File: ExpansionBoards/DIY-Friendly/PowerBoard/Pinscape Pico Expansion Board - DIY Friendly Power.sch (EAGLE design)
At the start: 75 parts, among them IC1 UCC27524P, IC10 ULN2803A, IC11 ULN2803A, IC12 ULN2803A, IC13 DS1307+, IC2 UCC27524P, IC3 UCC27524P, IC4 UCC27524P, IC5 UCC27524P, IC6 UCC27524P, IC7 UCC27524P, IC8 UCC27524P, IC9 ULN2803A, J1 640445-4, J15 SSQ-108-02-T-S-RA, J2 640445-9, J3 640445-9, J4 1-640456-0, J5 1-640456-0, J6 1-640456-0, J7 1-640456-0, Q1 FDPF085N10A, Q10 FDPF085N10A, Q11 FDPF085N10A, Q12 FDPF085N10A, Q13 FDPF085N10A, Q14 FDPF085N10A, Q15 FDPF085N10A, Q16 FDPF085N10A, Q2 FDPF085N10A, Q3 FDPF085N10A, Q4 FDPF085N10A, Q5 FDPF085N10A, Q6 FDPF085N10A, Q7 FDPF085N10A, Q8 FDPF085N10A, Q9 FDPF085N10A, Y1 ECS-.327-12.5-13X-C

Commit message: expansion board improvements
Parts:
- J1: value 640445-4 -> 640445-6; device SamacSys_Parts:640445-4 -> SamacSys_Parts:640445-6
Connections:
- net 12V: now also J1.5; no longer J1.3
- net 5V: now also J1.6; no longer J1.4
- net GND: now also J1.3, J1.4
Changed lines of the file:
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@@
 <attribute name="PARTNO" value="810-FG14X5R1H475KRT0"/>
 </part>
-<part name="J1" library="SamacSys_Parts" deviceset="640445-4" device=""/>
+<part name="J1" library="SamacSys_Parts" deviceset="640445-6" device=""/>
 <part name="J15" library="SamacSys_Parts" deviceset="SSQ-108-02-T-S-RA" device=""/>
 <part name="D2" library="SamacSys_Parts" deviceset="SB140-T" device=""/>
@@
 <text x="96.52" y="168.148" size="2.54" layer="91" align="center">Worker Pico 1</text>
 <text x="96.52" y="81.788" size="2.54" layer="91" align="center">Worker Pico 2</text>
-<text x="193.04" y="167.64" size="2.54" layer="91" align="center">Secondary PSU Power Input</text>
+<text x="193.04" y="172.72" size="2.54" layer="91" align="center">Secondary PSU Power Input</text>
 <text x="193.04" y="147.32" size="2.54" layer="91" align="center">Cross-Board Signals</text>
 </plain>
@@
 <instance part="PICO2" gate="G$1" x="96.52" y="45.72"/>
 <instance part="D1" gate="G$1" x="119.38" y="68.58"/>
-<instance part="J1" gate="G$1" x="182.88" y="162.56" smashed="yes">
-<attribute name="NAME" x="199.39" y="165.1" size="1.778" layer="95" align="center-left"/>
-<attribute name="VALUE" x="199.39" y="162.56" size="1.778" layer="96" align="center-left"/>
+<instance part="J1" gate="G$1" x="182.88" y="167.64" smashed="yes">
+<attribute name="NAME" x="199.39" y="170.18" size="1.778" layer="95" align="center-left"/>
+<attribute name="VALUE" x="199.39" y="167.64" size="1.778" layer="96" align="center-left"/>
 </instance>
 <instance part="J15" gate="G$1" x="182.88" y="139.7" smashed="yes">
@@
 <segment>
 <pinref part="J1" gate="G$1" pin="2"/>
-<wire x1="180.34" y1="160.02" x2="182.88" y2="160.02" width="0.1524" layer="91"/>
-<label x="177.8" y="162.56" size="1.27" layer="95" rot="R180" xref="yes"/>
+<wire x1="180.34" y1="165.1" x2="182.88" y2="165.1" width="0.1524" layer="91"/>
+<label x="177.8" y="167.64" size="1.27" layer="95" rot="R180" xref="yes"/>
 <pinref part="J1" gate="G$1" pin="1"/>
-<wire x1="177.8" y1="162.56" x2="180.34" y2="162.56" width="0.1524" layer="91"/>
+<wire x1="177.8" y1="167.64" x2="180.34" y2="167.64" width="0.1524" layer="91"/>
+<wire x1="180.34" y1="167.64" x2="182.88" y2="167.64" width="0.1524" layer="91"/>
+<wire x1="180.34" y1="167.64" x2="180.34" y2="165.1" width="0.1524" layer="91"/>
+<junction x="180.34" y="167.64"/>
+<wire x1="180.34" y1="165.1" x2="180.34" y2="162.56" width="0.1524" layer="91"/>
+<junction x="180.34" y="165.1"/>
+<pinref part="J1" gate="G$1" pin="3"/>
 <wire x1="180.34" y1="162.56" x2="182.88" y2="162.56" width="0.1524" layer="91"/>
 <wire x1="180.34" y1="162.56" x2="180.34" y2="160.02" width="0.1524" layer="91"/>
 <junction x="180.34" y="162.56"/>
+<pinref part="J1" gate="G$1" pin="4"/>
+<wire x1="180.34" y1="160.02" x2="182.88" y2="160.02" width="0.1524" layer="91"/>
 </segment>
 <segment>
@@
 <net name="5V" class="0">
 <segment>
-<pinref part="J1" gate="G$1" pin="4"/>
+<label x="180.34" y="154.94" size="1.27" layer="95" rot="R180" xref="yes"/>
+<pinref part="J1" gate="G$1" pin="6"/>
 <wire x1="180.34" y1="154.94" x2="182.88" y2="154.94" width="0.1524" layer="91"/>
-<label x="180.34" y="154.94" size="1.27" layer="95" rot="R180" xref="yes"/>
 </segment>
 </net>
 <net name="12V" class="0">
 <segment>
-<pinref part="J1" gate="G$1" pin="3"/>
+<label x="180.34" y="157.48" size="1.27" layer="95" rot="R180" xref="yes"/>
+<pinref part="J1" gate="G$1" pin="5"/>
 <wire x1="180.34" y1="157.48" x2="182.88" y2="157.48" width="0.1524" layer="91"/>
-<label x="180.34" y="157.48" size="1.27" layer="95" rot="R180" xref="yes"/>
-</segment>
-</net>
+</segment>
+</net>

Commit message: DIY board: individual reset buttons per Pico; swap cross-board connectors
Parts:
- removed J15: SSQ-108-02-T-S-RA, SamacSys_Parts:SSQ-108-02-T-S-RA
- added J8: (no value), pinhead:PINHD-1X8/90
- added Q17, Q18: 2N2222A, SamacSys_Parts:2N2222A
- added R13, R33: 2.2k, resistor:R-US_0204/7
- added R18, R32: 4.7K, resistor:R-US_0204/7
- added S1, S2: (no value), switch-omron:10-XX
- J1: value 640445-6 -> 640445-9; device SamacSys_Parts:640445-6 -> SamacSys_Parts:640445-9
- J3: value 640445-9 -> 640445-6; device SamacSys_Parts:640445-9 -> SamacSys_Parts:640445-6
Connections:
- removed net /RESET: J15.2, PICO1.RUN, PICO2.RUN
- new net /PERIPHERAL_POWER_ENABLE: J8.7, R13.1, R33.1
- new net N$38: PICO2.3V3, R32.2
- new net N$39: Q17.B, R33.2
- new net N$40: PICO2.RUN, Q17.C, R32.1, S2.P, S2.P1
- new net N$41: PICO1.3V3, R18.2
- new net N$42: Q18.B, R13.2
- new net N$51: PICO1.RUN, Q18.C, R18.1, S1.P, S1.P1
- net 12V: now also J3.5; no longer J1.5
- net 5V: now also J3.6; no longer J1.6
- net GND: now also J3.1, J3.2, J3.3, J3.4, J8.2, J8.4, J8.6, J8.8, Q17.E, Q18.E, S1.S, S1.S1, S2.S, S2.S1; no longer J1.1, J1.2, J1.3, J1.4, J15.1, J15.3, J15.5, J15.7
- net OUT13: now also J1.1; no longer J2.1
- net OUT14: now also J1.2; no longer J2.2
- net OUT15: now also J1.4; no longer J2.4
- net OUT16: now also J1.5; no longer J2.5
- net OUT17: now also J1.6; no longer J2.6
- net OUT18: now also J1.7; no longer J2.7
- net OUT19: now also J1.8; no longer J2.8
- net OUT20: now also J1.9; no longer J2.9
- net OUT21: now also J2.1; no longer J3.1
- net OUT22: now also J2.2; no longer J3.2
- net OUT23: now also J2.3; no longer J3.3
- net OUT24: now also J2.5; no longer J3.5
- net OUT25: now also J2.6; no longer J3.6
- net OUT26: now also J2.7; no longer J3.7
- net OUT27: now also J2.8; no longer J3.8
- net OUT28: now also J2.9; no longer J3.9
- net SCL: now also J8.3; no longer J15.6
- net SDA: now also J8.5; no longer J15.4
- net VBUS: now also J8.1; no longer J15.8
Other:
- note added: "Pico 2 Reset"

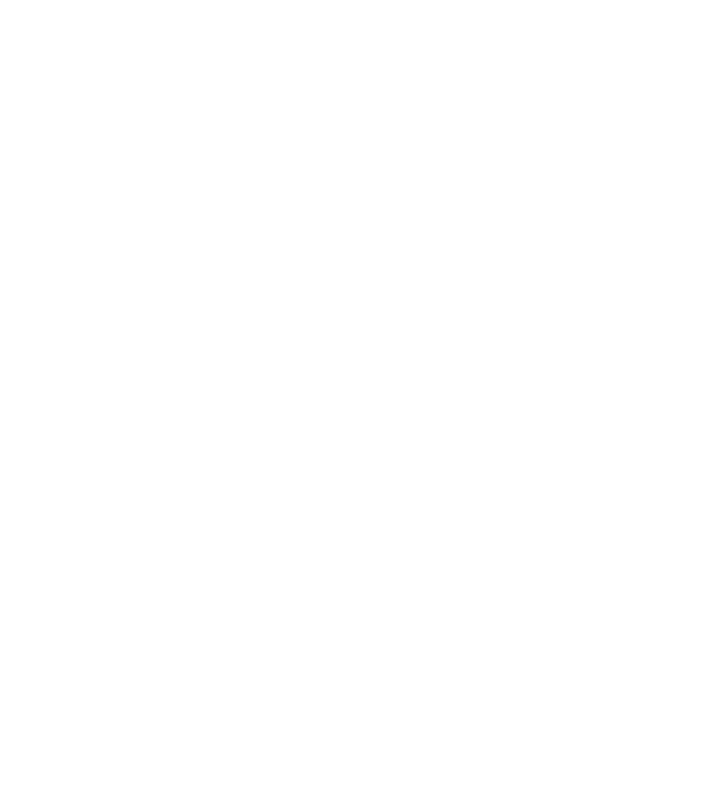
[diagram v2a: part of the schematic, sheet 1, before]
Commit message: KL25Z adapters - connect AGND to GND
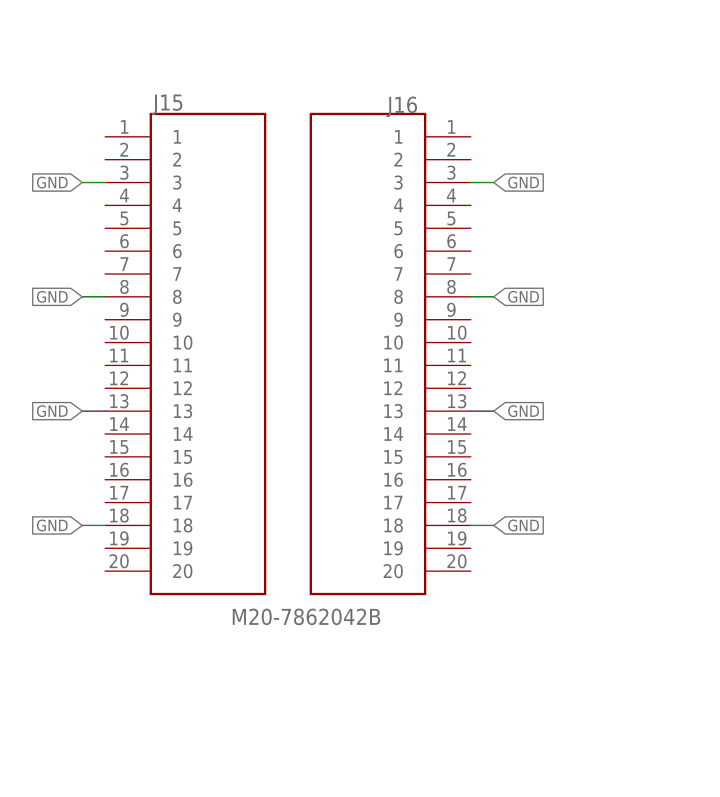
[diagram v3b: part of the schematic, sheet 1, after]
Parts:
- added J15, J16: M20-7862042B, SamacSys_Parts:M20-7862042B
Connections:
- net GND: now also J15.13, J15.18, J15.3, J15.8, J16.13, J16.18, J16.3, J16.8
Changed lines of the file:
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@@
 <part name="S1" library="switch-omron" deviceset="10-XX" device=""/>
 <part name="GND5" library="supply1" deviceset="GND" device=""/>
+<part name="J15" library="SamacSys_Parts" deviceset="M20-7862042" device="B" value="M20-7862042B"/>
+<part name="J16" library="SamacSys_Parts" deviceset="M20-7862042" device="B" value="M20-7862042B"/>
 </parts>
 <sheets>
@@
 <instance part="S1" gate="1" x="119.38" y="121.92" rot="R270"/>
 <instance part="GND5" gate="1" x="129.54" y="121.92" rot="R90"/>
+<instance part="J15" gate="G$1" x="-88.9" y="147.32" smashed="yes">
+<attribute name="NAME" x="-83.566" y="151.13" size="1.778" layer="95" align="center-left"/>
+<attribute name="VALUE" x="-74.93" y="93.98" size="1.778" layer="96" align="center-left"/>
+</instance>
+<instance part="J16" gate="G$1" x="-48.26" y="147.32" smashed="yes" rot="MR0">
+<attribute name="NAME" x="-54.102" y="150.876" size="1.778" layer="95" rot="MR0" align="center-left"/>
+</instance>
 </instances>
 <busses>
@@
 <pinref part="GND5" gate="1" pin="GND"/>
 </segment>
+<segment>
+<pinref part="J15" gate="G$1" pin="3"/>
+<wire x1="-91.44" y1="142.24" x2="-88.9" y2="142.24" width="0.1524" layer="91"/>
+<label x="-91.44" y="142.24" size="1.27" layer="95" rot="R180" xref="yes"/>
+</segment>
+<segment>
+<label x="-91.44" y="129.54" size="1.27" layer="95" rot="R180" xref="yes"/>
+<pinref part="J15" gate="G$1" pin="8"/>
+<wire x1="-91.44" y1="129.54" x2="-88.9" y2="129.54" width="0.1524" layer="91"/>
+</segment>
+<segment>
+<label x="-91.44" y="104.14" size="1.27" layer="95" rot="R180" xref="yes"/>
+<pinref part="J15" gate="G$1" pin="18"/>
+<wire x1="-91.44" y1="104.14" x2="-88.9" y2="104.14" width="0.1524" layer="91"/>
+</segment>
+<segment>
+<label x="-45.72" y="104.14" size="1.27" layer="95" xref="yes"/>
+<pinref part="J16" gate="G$1" pin="18"/>
+<wire x1="-48.26" y1="104.14" x2="-45.72" y2="104.14" width="0.1524" layer="91"/>
+</segment>
+<segment>
+<label x="-45.72" y="116.84" size="1.27" layer="95" xref="yes"/>
+<pinref part="J16" gate="G$1" pin="13"/>
+<wire x1="-48.26" y1="116.84" x2="-45.72" y2="116.84" width="0.1524" layer="91"/>
+</segment>
+<segment>
+<label x="-45.72" y="129.54" size="1.27" layer="95" xref="yes"/>
+<pinref part="J16" gate="G$1" pin="8"/>
+<wire x1="-48.26" y1="129.54" x2="-45.72" y2="129.54" width="0.1524" layer="91"/>
+</segment>
+<segment>
+<label x="-45.72" y="142.24" size="1.27" layer="95" xref="yes"/>
+<pinref part="J16" gate="G$1" pin="3"/>
+<wire x1="-48.26" y1="142.24" x2="-45.72" y2="142.24" width="0.1524" layer="91"/>
+</segment>
+<segment>
+<pinref part="J15" gate="G$1" pin="13"/>
+<wire x1="-91.44" y1="116.84" x2="-88.9" y2="116.84" width="0.1524" layer="91"/>
+<label x="-91.44" y="116.84" size="1.27" layer="95" rot="R180" xref="yes"/>
+</segment>
 </net>
